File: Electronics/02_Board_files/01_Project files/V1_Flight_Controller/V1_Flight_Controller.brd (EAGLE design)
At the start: 46.2 x 46.2 mm, 81 parts

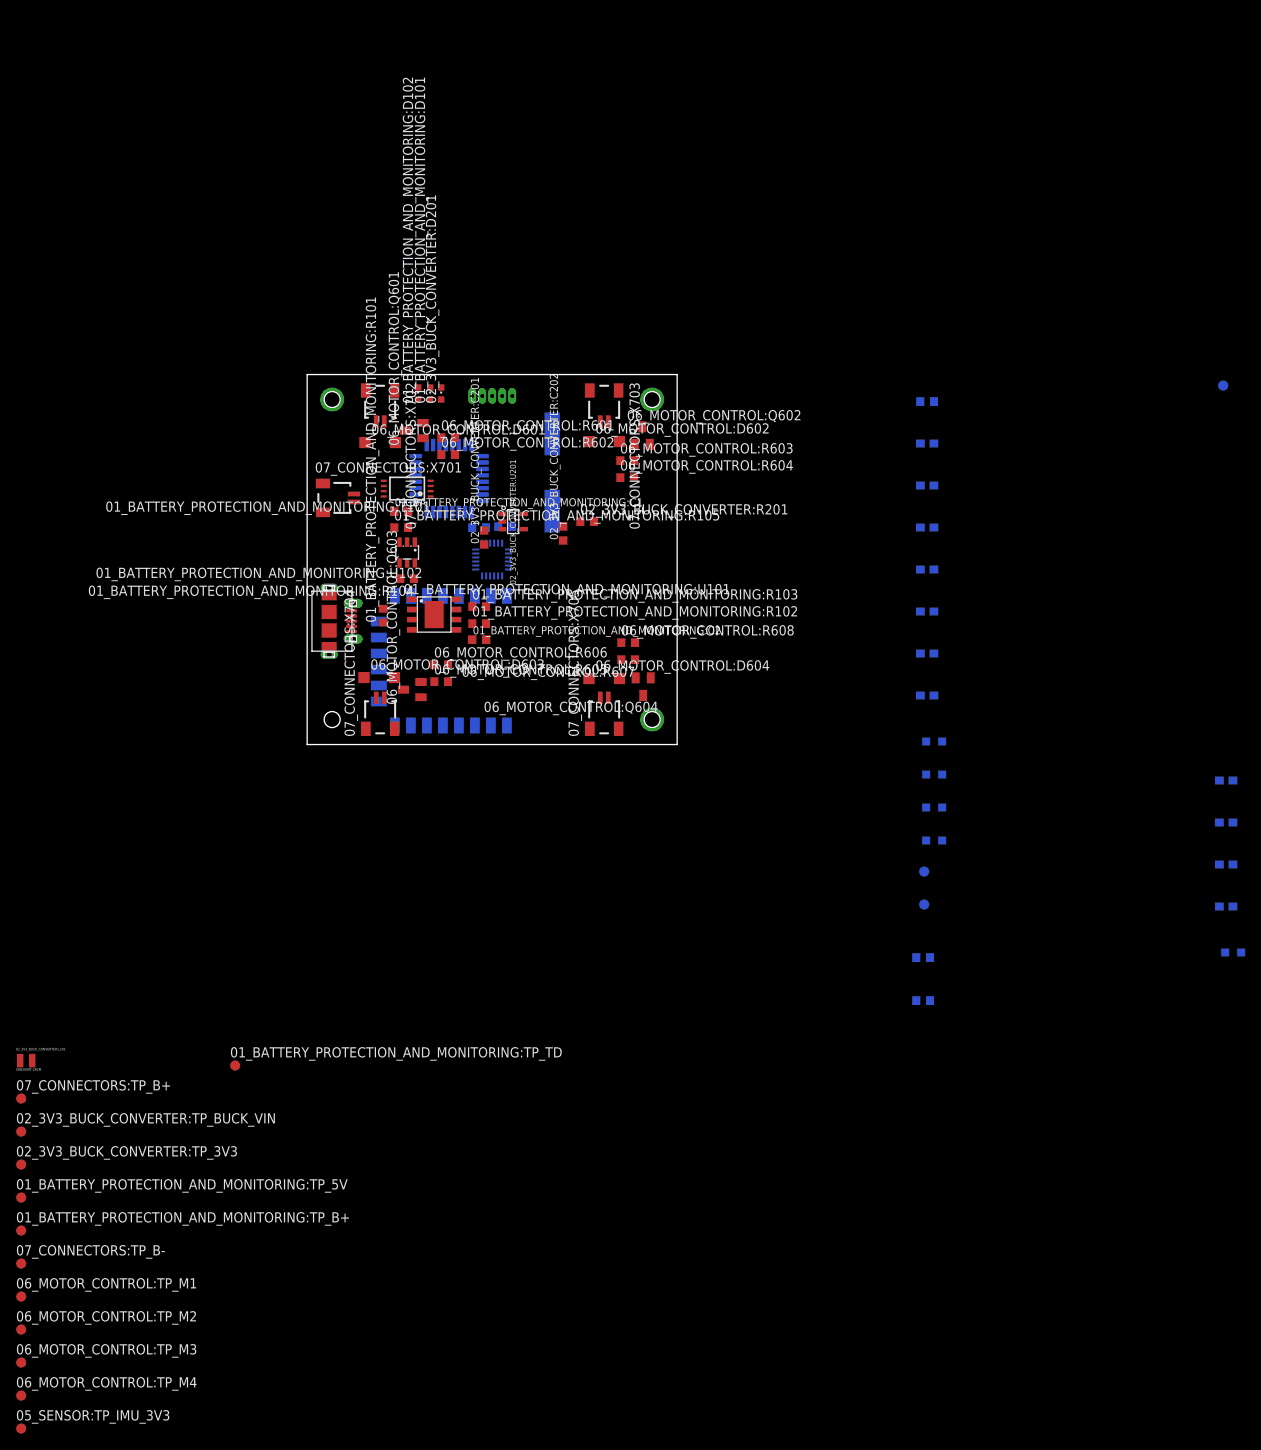
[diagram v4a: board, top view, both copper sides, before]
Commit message: 1. 80% placement and 50% routing completed 2. Removed central two layers making the pcb a 2 layer pcb 3. Added resists in MPU-6050.lbr 4. Added dimensions in SRN2009T-2R2M.lbr
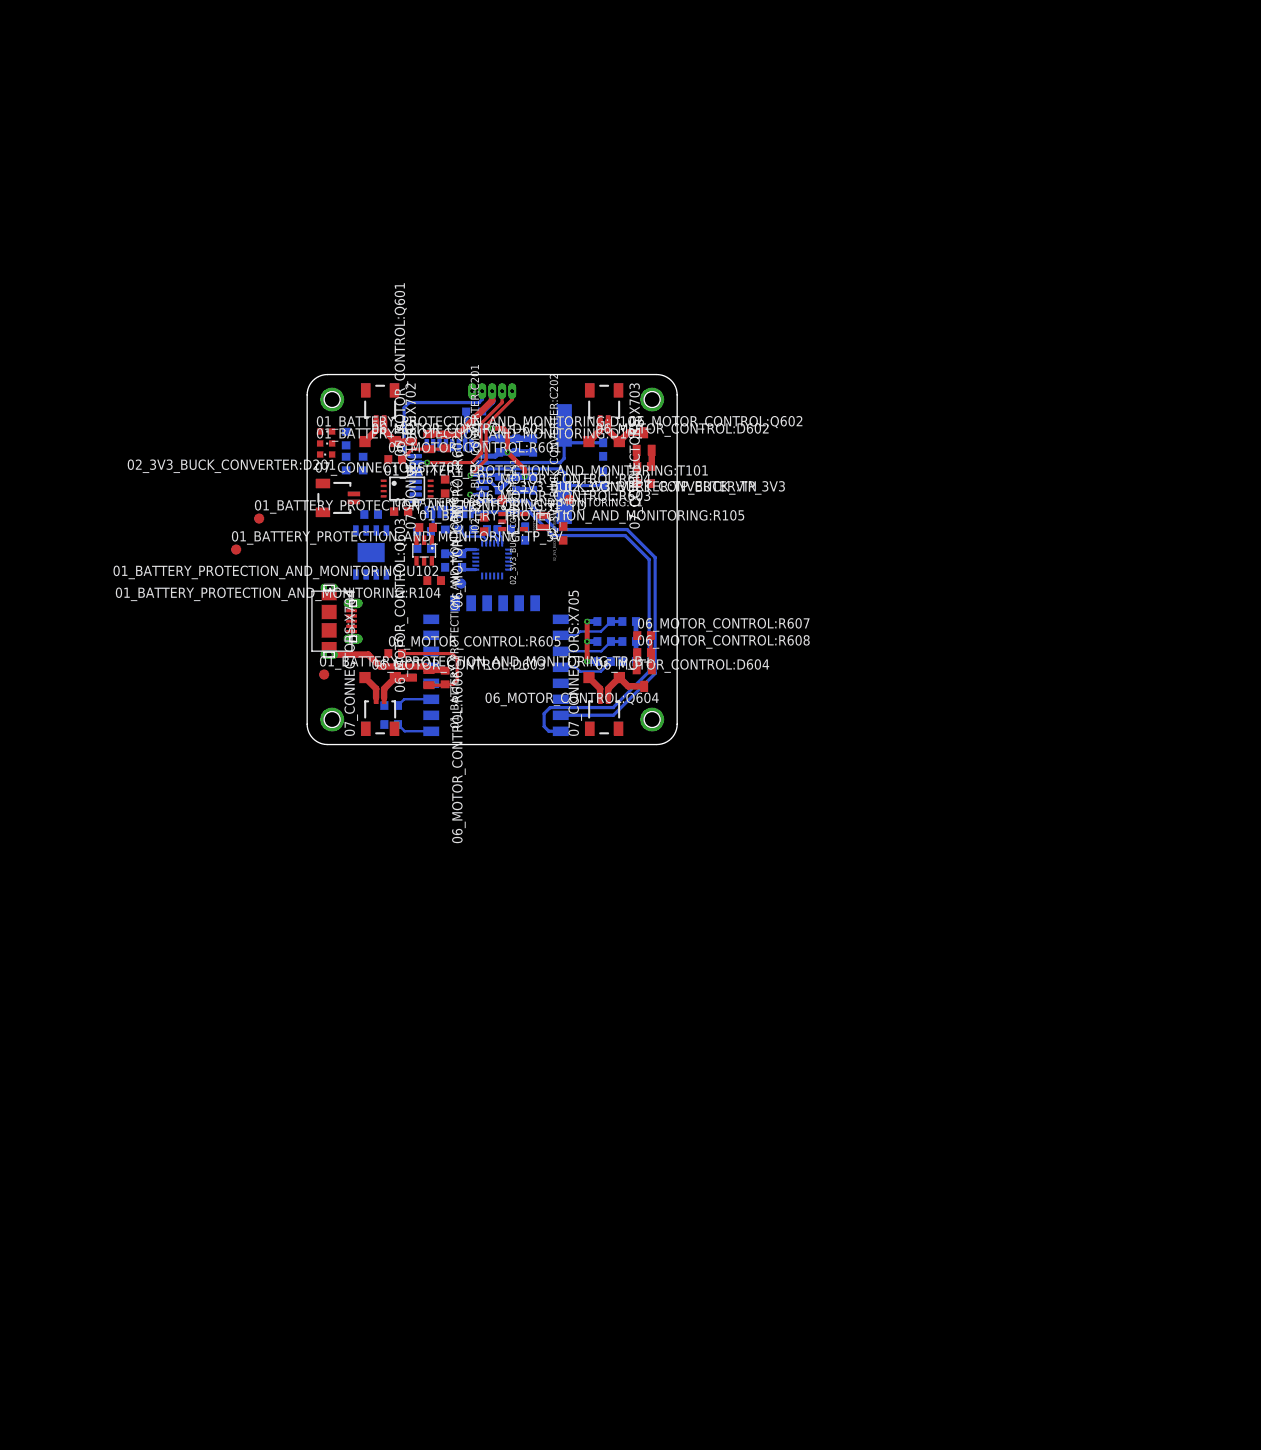
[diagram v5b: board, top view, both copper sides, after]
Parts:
- removed 03_MICROCONTROLLER:L301, 03_MICROCONTROLLER:L304, 05_SENSOR:L501: (no value), rcl:L2012C
- removed 03_MICROCONTROLLER:TP_MCU_3V3, 03_MICROCONTROLLER:TP_SCL, 03_MICROCONTROLLER:TP_SDA, 06_MOTOR_CONTROL:TP_M1, 06_MOTOR_CONTROL:TP_M2, 06_MOTOR_CONTROL:TP_M3, 06_MOTOR_CONTROL:TP_M4, 07_CONNECTORS:TP_B+, 07_CONNECTORS:TP_B-: TPB1,27, testpad:B1,27
- added 04_WIFI:R401, 04_WIFI:R402, 04_WIFI:R403, 04_WIFI:R404, 04_WIFI:R405, 04_WIFI:R406, 04_WIFI:R407, 04_WIFI:R408: 10KΩ, adafruit:R0603
- 01_BATTERY_PROTECTION_AND_MONITORING:R101: value 1.2KΩ -> 4.8KΩ
- moved 05_SENSOR:TP_IMU_3V3 119.1 mm to (19.2, 20.1), flipped to the bottom
- moved 02_3V3_BUCK_CONVERTER:TP_3V3 107.7 mm to (32.8, 30.6)
- moved 05_SENSOR:C504 106.8 mm to (17.2, 23.0), turned to 90 degrees
- moved 05_SENSOR:C502 102.8 mm to (19.4, 23.0), turned to 90 degrees
- moved 05_SENSOR:C503 101.7 mm to (18.1, 26.9)
- moved 02_3V3_BUCK_CONVERTER:TP_BUCK_VIN 99.3 mm to (24.4, 30.6)
- moved 05_SENSOR:C501 94.8 mm to (27.2, 26.4), turned to 270 degrees
- moved 02_3V3_BUCK_CONVERTER:L201 93.4 mm to (29.5, 27.9), turned to 270 degrees
- moved 01_BATTERY_PROTECTION_AND_MONITORING:TP_5V 85.3 mm to (-8.88, 24.4)
- moved 03_MICROCONTROLLER:R303 84.2 mm to (14.6, 24.5), turned to 180 degrees
- moved 03_MICROCONTROLLER:R302 82.0 mm to (14.6, 26.6)
- moved 01_BATTERY_PROTECTION_AND_MONITORING:TP_B+ 79.2 mm to (2.12, 8.75)
- moved 03_MICROCONTROLLER:L303 75.9 mm to (20.9, 41.6), turned to 180 degrees
- moved 03_MICROCONTROLLER:L302 72.0 mm to (20.9, 39.5), turned to 180 degrees
- moved 01_BATTERY_PROTECTION_AND_MONITORING:TP_TD 68.4 mm to (-6.00, 28.2)
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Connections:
- net 02_3V3_BUCK_CONVERTER:N$1 renamed 02_3V3_BUCK_CONVERTER:SW
- net 02_3V3_BUCK_CONVERTER:N$2 renamed 02_3V3_BUCK_CONVERTER:LED_3V3
- net 05_SENSOR:N$1 renamed 05_SENSOR:REGOUT
- net 05_SENSOR:N$2 renamed 05_SENSOR:CPOUT
- net 06_MOTOR_CONTROL:N$1 renamed 06_MOTOR_CONTROL:M2_GATE
- net 06_MOTOR_CONTROL:N$2 renamed 06_MOTOR_CONTROL:M1_GATE
- net 06_MOTOR_CONTROL:N$3 renamed 06_MOTOR_CONTROL:M3_GATE
- net 06_MOTOR_CONTROL:N$4 renamed 06_MOTOR_CONTROL:M4_GATE
- removed net 03_MICROCONTROLLER:3V3_MCU: 03_MICROCONTROLLER:C301.1, 03_MICROCONTROLLER:C302.1, 03_MICROCONTROLLER:C303.1, 03_MICROCONTROLLER:L301.1, 03_MICROCONTROLLER:L302.2, 03_MICROCONTROLLER:L304.1, 03_MICROCONTROLLER:R301.1, 03_MICROCONTROLLER:TP_MCU_3V3.TP, 03_MICROCONTROLLER:U301.1, 03_MICROCONTROLLER:U301.17
- removed net 03_MICROCONTROLLER:GND_MCU: 03_MICROCONTROLLER:C301.2, 03_MICROCONTROLLER:C302.2, 03_MICROCONTROLLER:C303.2, 03_MICROCONTROLLER:C304.2, 03_MICROCONTROLLER:C305.2, 03_MICROCONTROLLER:C306.2, 03_MICROCONTROLLER:C307.2, 03_MICROCONTROLLER:L303.2, 03_MICROCONTROLLER:R303.1, 03_MICROCONTROLLER:U301.16, 03_MICROCONTROLLER:U301.32
- removed net 03_MICROCONTROLLER:VBAT_LEVEL: 03_MICROCONTROLLER:R302.2
- removed net 03_MICROCONTROLLER:VDDA: 03_MICROCONTROLLER:C304.1, 03_MICROCONTROLLER:C305.1, 03_MICROCONTROLLER:L304.2, 03_MICROCONTROLLER:U301.5
- removed net 04_WIFI:3V3_ESP8266: 04_WIFI:U401.8
- removed net 04_WIFI:GND_ESP8266: 04_WIFI:U401.9
- removed net 05_SENSOR:3V3_IMU: 05_SENSOR:C501.1, 05_SENSOR:C502.1, 05_SENSOR:L501.1, 05_SENSOR:R501.1, 05_SENSOR:R502.1, 05_SENSOR:TP_IMU_3V3.TP, 05_SENSOR:U501.13, 05_SENSOR:U501.8
- removed net 05_SENSOR:GND_IMU: 05_SENSOR:C501.2, 05_SENSOR:C502.2, 05_SENSOR:C503.2, 05_SENSOR:C504.2, 05_SENSOR:U501.1, 05_SENSOR:U501.11, 05_SENSOR:U501.18, 05_SENSOR:U501.9
- new net 04_WIFI:CH_PD: 04_WIFI:R402.2, 04_WIFI:U401.3
- new net 04_WIFI:GPIO0: 04_WIFI:R403.2, 04_WIFI:R404.1, 04_WIFI:U401.12
- new net 04_WIFI:GPIO15: 04_WIFI:R407.2, 04_WIFI:R408.1, 04_WIFI:U401.10
- new net 04_WIFI:GPIO2: 04_WIFI:R405.2, 04_WIFI:R406.1, 04_WIFI:U401.11
- net +3V3: now also 03_MICROCONTROLLER:C301.1, 03_MICROCONTROLLER:C302.1, 03_MICROCONTROLLER:C303.1, 03_MICROCONTROLLER:C304.1, 03_MICROCONTROLLER:C305.1, 03_MICROCONTROLLER:L302.2, 03_MICROCONTROLLER:R301.1, 03_MICROCONTROLLER:U301.1, 03_MICROCONTROLLER:U301.17, 03_MICROCONTROLLER:U301.5, 04_WIFI:R401.1, 04_WIFI:R402.1, 04_WIFI:R403.1, 04_WIFI:R405.1, 04_WIFI:R407.1, 04_WIFI:U401.8, 05_SENSOR:C501.1, 05_SENSOR:C502.1, 05_SENSOR:R501.1, 05_SENSOR:R502.1, 05_SENSOR:TP_IMU_3V3.TP, 05_SENSOR:U501.13, 05_SENSOR:U501.8, 07_CONNECTORS:X706.5; no longer 03_MICROCONTROLLER:L301.2, 05_SENSOR:L501.2, 07_CONNECTORS:X706.1
- net 03_MICROCONTROLLER:BAT_MON: now also 03_MICROCONTROLLER:U301.15; no longer 03_MICROCONTROLLER:U301.6
- net BATTERY_+VE: now also 03_MICROCONTROLLER:R302.2, 07_CONNECTORS:X702.2, 07_CONNECTORS:X703.2; no longer 06_MOTOR_CONTROL:TP_M1.TP, 06_MOTOR_CONTROL:TP_M2.TP, 06_MOTOR_CONTROL:TP_M3.TP, 06_MOTOR_CONTROL:TP_M4.TP, 07_CONNECTORS:TP_B+.TP, 07_CONNECTORS:X702.1, 07_CONNECTORS:X703.1
- net BATTERY_-VE: no longer 07_CONNECTORS:TP_B-.TP
- net ESP8266_RST: now also 04_WIFI:R401.2
- net GND: now also 03_MICROCONTROLLER:C301.2, 03_MICROCONTROLLER:C302.2, 03_MICROCONTROLLER:C303.2, 03_MICROCONTROLLER:C304.2, 03_MICROCONTROLLER:C305.2, 03_MICROCONTROLLER:C306.2, 03_MICROCONTROLLER:C307.2, 03_MICROCONTROLLER:L303.2, 03_MICROCONTROLLER:R303.1, 03_MICROCONTROLLER:U301.16, 03_MICROCONTROLLER:U301.32, 04_WIFI:R404.2, 04_WIFI:R406.2, 04_WIFI:R408.2, 04_WIFI:U401.9, 05_SENSOR:C501.2, 05_SENSOR:C502.2, 05_SENSOR:C503.2, 05_SENSOR:C504.2, 05_SENSOR:U501.1, 05_SENSOR:U501.11, 05_SENSOR:U501.18, 05_SENSOR:U501.9
- net I2C_SCL: no longer 03_MICROCONTROLLER:TP_SCL.TP
- net I2C_SDA: no longer 03_MICROCONTROLLER:TP_SDA.TP
- net M1: now also 07_CONNECTORS:X702.1; no longer 07_CONNECTORS:X702.2
- net M2: now also 07_CONNECTORS:X703.1; no longer 07_CONNECTORS:X703.2
- net NRST: now also 07_CONNECTORS:X706.1; no longer 07_CONNECTORS:X706.5
- net SWCLK: now also 07_CONNECTORS:X706.4; no longer 07_CONNECTORS:X706.2
- net SWDIO: now also 07_CONNECTORS:X706.2; no longer 07_CONNECTORS:X706.4
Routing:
- net UART1_RX: track 0.00 -> 57.9 mm
- net UART1_TX: track 0.00 -> 53.0 mm
- net GND: track 0.00 -> 52.6 mm
- net +3V3: track 0.00 -> 34.5 mm, vias 0 -> 6
- net 03_MICROCONTROLLER:XTAL_IN: track 0.00 -> 19.4 mm
- net 03_MICROCONTROLLER:XTAL_OUT: track 0.00 -> 19.0 mm
- net SWCLK: track 0.00 -> 18.4 mm
- net SWDIO: track 0.00 -> 17.5 mm, vias 0 -> 1
- net NRST: track 0.00 -> 16.4 mm, vias 0 -> 1
- net 06_MOTOR_CONTROL:M3_GATE: track 0.00 -> 13.7 mm
- net BATTERY_+VE: track 0.00 -> 12.4 mm
- net 04_WIFI:GPIO15: track 0.00 -> 8.41 mm
- net 04_WIFI:GPIO2: track 0.00 -> 8.20 mm
- net 04_WIFI:GPIO0: track 0.00 -> 7.01 mm
- net M4: track 0.00 -> 6.66 mm
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- removed copper zone on layer 15, net GND
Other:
- outline, holes or cut-outs redrawn

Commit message: 1. Routing
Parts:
- removed 01_BATTERY_PROTECTION_AND_MONITORING:TP_B+, 02_3V3_BUCK_CONVERTER:TP_3V3, 02_3V3_BUCK_CONVERTER:TP_BUCK_VIN: TPB1,27, testpad:B1,27
- moved 01_BATTERY_PROTECTION_AND_MONITORING:TP_TD 20.3 mm to (13.6, 22.9)
- moved 01_BATTERY_PROTECTION_AND_MONITORING:TP_5V 14.6 mm to (5.50, 21.9)
- moved 01_BATTERY_PROTECTION_AND_MONITORING:C1 10.4 mm to (18.1, 20.9)
- moved 01_BATTERY_PROTECTION_AND_MONITORING:R103 2.30 mm to (6.50, 39.9)
- moved 01_BATTERY_PROTECTION_AND_MONITORING:R101 1.95 mm to (9.25, 27.2)
- moved 01_BATTERY_PROTECTION_AND_MONITORING:U101 1.80 mm to (9.00, 22.5)
- moved 01_BATTERY_PROTECTION_AND_MONITORING:R102 1.64 mm to (8.62, 35.4)
- moved 02_3V3_BUCK_CONVERTER:R201 1.64 mm to (6.50, 35.4)
- moved 01_BATTERY_PROTECTION_AND_MONITORING:R105 1.60 mm to (16.1, 28.1), turned to 270 degrees
- moved 01_BATTERY_PROTECTION_AND_MONITORING:C2 1.25 mm to (18.5, 32.2)
- moved 01_BATTERY_PROTECTION_AND_MONITORING:T101 1.25 mm to (13.8, 32.0)
- moved 01_BATTERY_PROTECTION_AND_MONITORING:U102 1.25 mm to (15.9, 24.2)
- moved 01_BATTERY_PROTECTION_AND_MONITORING:R104 0.95 mm to (15.0, 20.9)
- moved 06_MOTOR_CONTROL:R604 0.75 mm to (42.1, 34.0)
- moved 06_MOTOR_CONTROL:R603 0.38 mm to (42.1, 32.2)
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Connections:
- net +3V3: no longer 02_3V3_BUCK_CONVERTER:TP_3V3.TP
- net BATTERY_+VE: no longer 01_BATTERY_PROTECTION_AND_MONITORING:TP_B+.TP, 02_3V3_BUCK_CONVERTER:TP_BUCK_VIN.TP
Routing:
- net BATTERY_+VE: track 12.4 -> 145.4 mm, vias 0 -> 3
- net GND: track 52.6 -> 120.5 mm, vias 0 -> 1
- net +5V: track 0.00 -> 49.3 mm, vias 0 -> 4
- net 01_BATTERY_PROTECTION_AND_MONITORING:CHRG: track 0.00 -> 28.7 mm, vias 0 -> 2
- net 01_BATTERY_PROTECTION_AND_MONITORING:STDBY: track 0.00 -> 23.9 mm, vias 0 -> 2
- net 01_BATTERY_PROTECTION_AND_MONITORING:OD: track 0.00 -> 13.1 mm
- net BATTERY_-VE: track 0.00 -> 10.2 mm
- net 01_BATTERY_PROTECTION_AND_MONITORING:OC: track 0.00 -> 6.80 mm
- net 01_BATTERY_PROTECTION_AND_MONITORING:STDBY_LED: track 0.00 -> 5.95 mm, vias 0 -> 1
- net 01_BATTERY_PROTECTION_AND_MONITORING:N$6: track 0.00 -> 5.85 mm
- net 01_BATTERY_PROTECTION_AND_MONITORING:CHRG_LED: track 0.00 -> 4.13 mm, vias 0 -> 1
- net 01_BATTERY_PROTECTION_AND_MONITORING:VCC: track 0.00 -> 3.49 mm
- net 02_3V3_BUCK_CONVERTER:LED_3V3: track 0.00 -> 3.26 mm, vias 0 -> 1
- net +3V3: track 34.5 -> 36.9 mm
- net 01_BATTERY_PROTECTION_AND_MONITORING:PROG: track 0.00 -> 2.01 mm
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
